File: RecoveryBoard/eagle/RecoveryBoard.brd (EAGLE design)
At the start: 120.9 x 54.6 mm, 96 parts, among them Q1 BSS123, Q2 BSS123, Q3 BSS123, Q4 BPR-301, Q5 BPR-301, Q6 MOSFET-PCH-SOT23-6, U1 STM32F042K6, U10 TPS63070, U2 BD62120AEFJ-E2, Y1 ECS-160-10-36Q-ES-TR

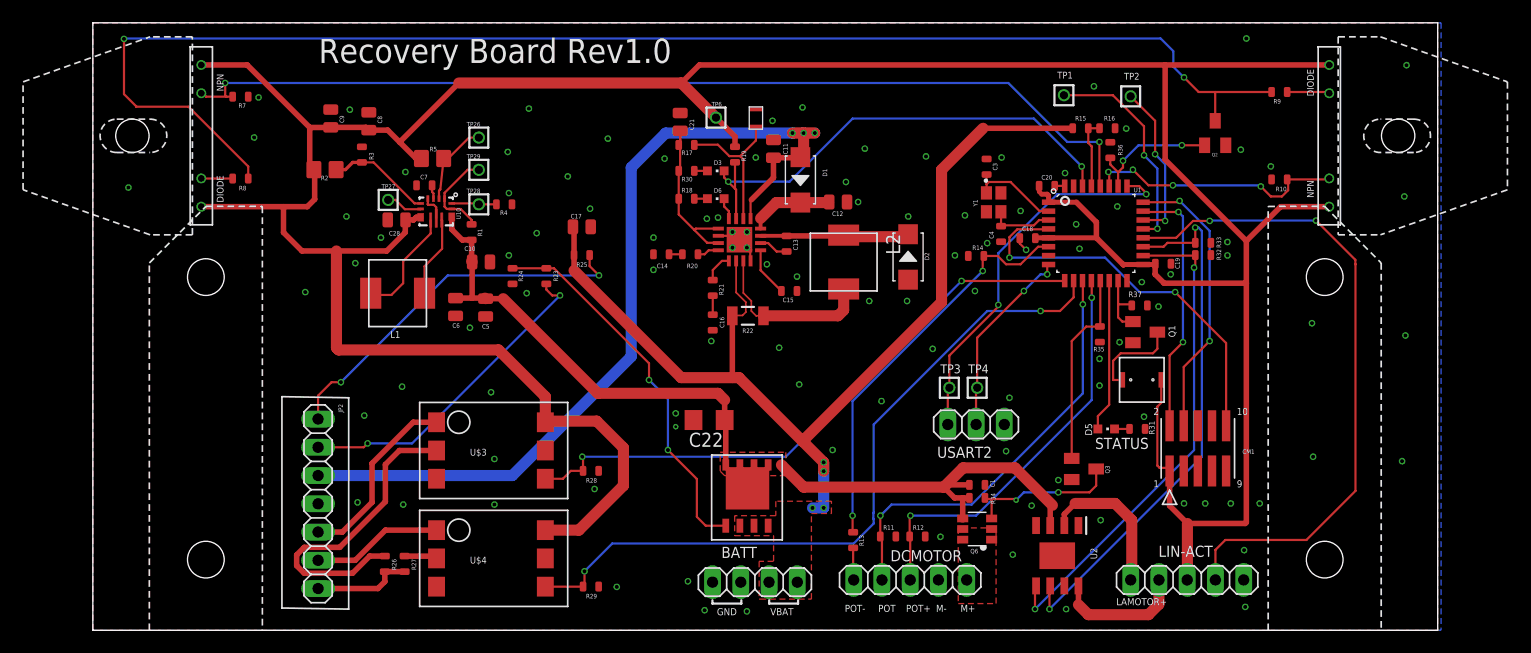
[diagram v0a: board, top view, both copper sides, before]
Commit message: Layout cleanup of RecoveryBoard for manufacturing. Sent off to Fab as v1.0
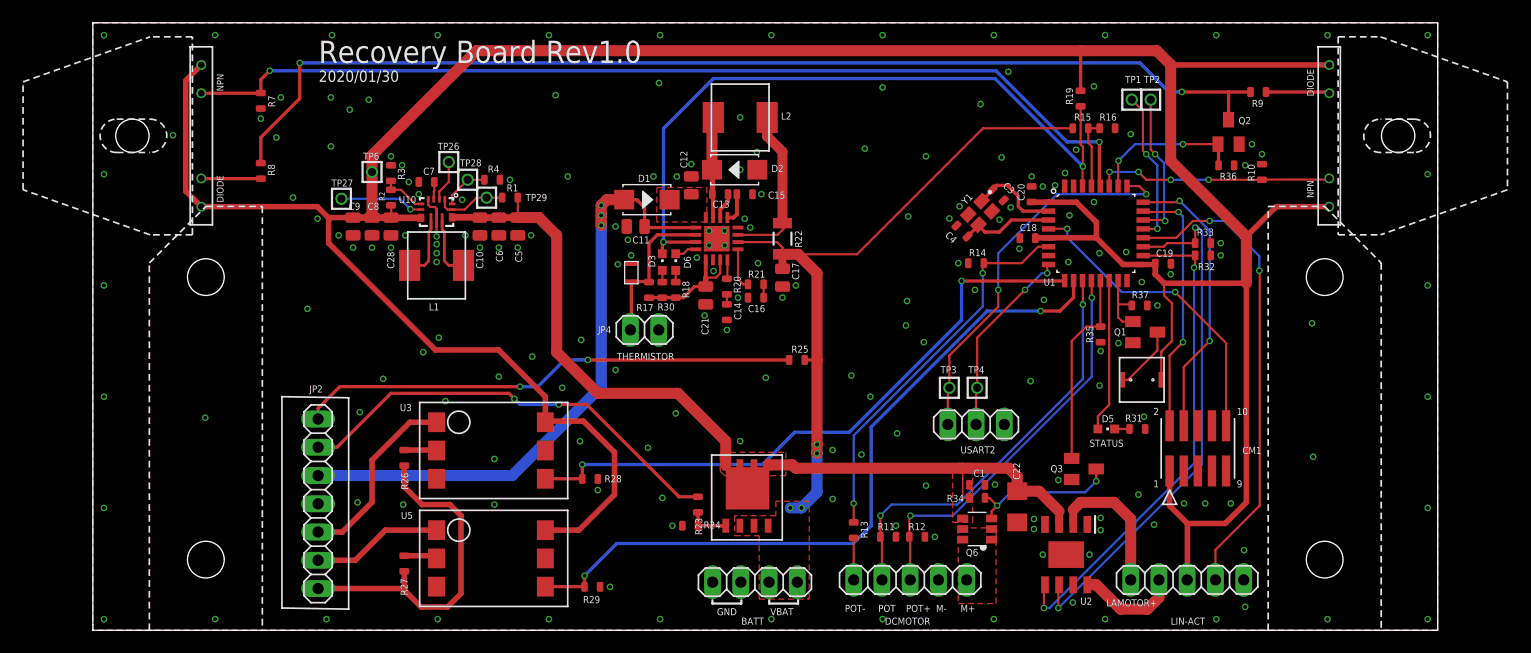
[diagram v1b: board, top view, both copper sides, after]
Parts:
- removed R5: 100k, oresat-rcl:.0805-A-NOSILK
- added JP4: (no value), pinhead:1X02
- C22: value 100n -> 10u
- R2: device oresat-rcl:.0805-A-NOSILK -> oresat-rcl:.0603-C-NOSILK
- moved R19 31.5 mm to (88.8, 47.8)
- moved TP6 31.3 mm to (25.1, 41.2)
- moved C22 28.8 mm to (83.1, 11.1), turned to 270 degrees
- moved R24 27.5 mm to (53.7, 9.40), turned to 0 degrees
- moved R23 24.7 mm to (54.4, 11.3), turned to 90 degrees
- moved R25 21.5 mm to (63.3, 24.3), turned to 0 degrees
- moved C17 18.6 mm to (62.0, 31.7), turned to 270 degrees
- moved U$6 17.9 mm to (48.4, 32.1)
- moved D2 17.5 mm to (57.7, 41.4), turned to 180 degrees
- moved L2 16.0 mm to (58.2, 46.1), turned to 0 degrees
- moved C21 15.8 mm to (55.1, 30.1), turned to 270 degrees
- moved C11 14.2 mm to (48.8, 36.3), turned to 180 degrees
- moved D1 13.9 mm to (49.8, 38.7), turned to 0 degrees
- moved R17 13.5 mm to (50.0, 30.6), turned to 270 degrees
- moved C12 13.3 mm to (53.8, 40.0), turned to 90 degrees
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- renumbered U$3 to U3, U$4 to U5
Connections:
- removed net N$3: U2.7
- net 3.3V: no longer R5.2
- net GND: now also JP4.2, U2.7
- net N$20: now also JP4.1
- net TPS-PG: no longer R5.1
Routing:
- net VBAT: track 94.3 -> 63.9 mm
- net N$16: track 34.3 -> 4.40 mm, vias 2 -> 0
- net N$27: track 128.5 -> 99.5 mm
- net N$7: track 28.2 -> 2.97 mm
- net VUMB: track 80.4 -> 57.6 mm
- net T_GND: track 8.94 -> 30.8 mm
- net 3.3V: track 311.3 -> 289.8 mm
- net ACOK: track 44.8 -> 64.3 mm
- net POT_OUT_AN: track 59.4 -> 43.2 mm
- net ARM-OUT: track 34.0 -> 45.1 mm
- net ARM-IN: track 29.4 -> 40.0 mm
- net !BEN: track 7.70 -> 0.00 mm
- net NRST: track 35.8 -> 28.2 mm
- net CAN_RX: track 19.3 -> 13.8 mm
- net TPS-FB: track 9.40 -> 4.03 mm
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- added copper zone on layer 1, net !BEN
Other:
- board text added: "2020/01/30"
- board text added: "THERMISTOR"
- board text removed: "TODO 1. I have CAN and USART Pins currenlty doing nothing 2. Need to add locking button"
